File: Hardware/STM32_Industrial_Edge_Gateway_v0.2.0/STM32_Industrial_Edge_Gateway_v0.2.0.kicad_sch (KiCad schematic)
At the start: 75 parts, among them J1 DC Barrel Jack (5.5 × 2.1mm), J2 Conn_01x05, J3 Conn_01x02, J4 RJ45_Hanrun_HR911105A_Horizon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, J5 Screw_Terminal_01x02, J6 DM3AT-SF-PEJM5, Q1 AO3407A, SW1 SW_Push, U1 MP2338GTL, U2 TLV76733DRVR, U3 STM32F407VGTx, U4 SMD3225, U5 LAN8742A, U6 MAX3485ESA_T, Y1 ABM8G-25.000MHZ-B4Y-T3

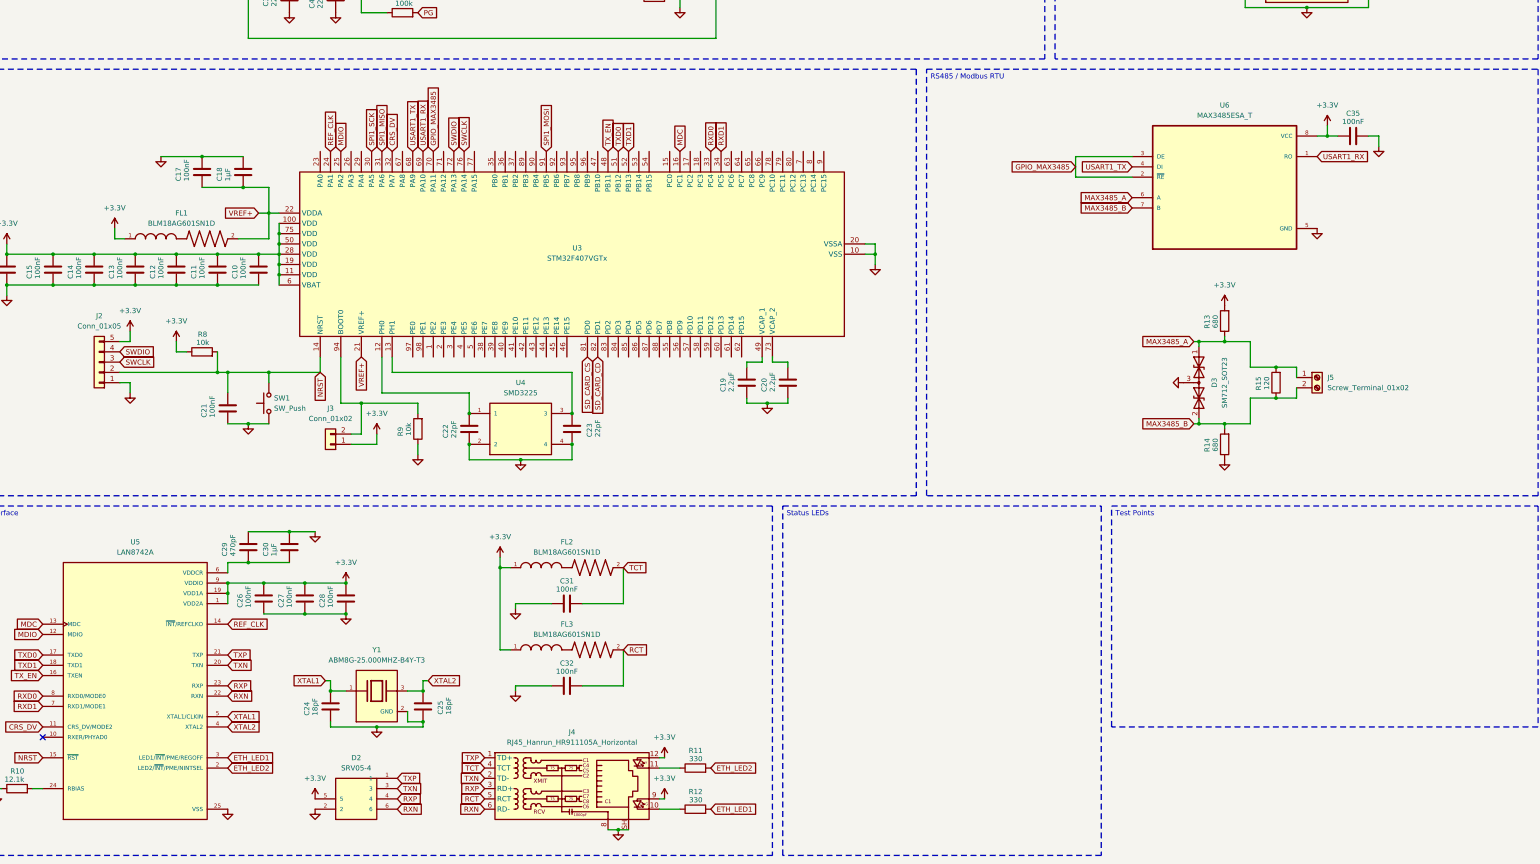
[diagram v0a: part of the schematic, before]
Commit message: Complete Testing Points and Status LEDs schematics
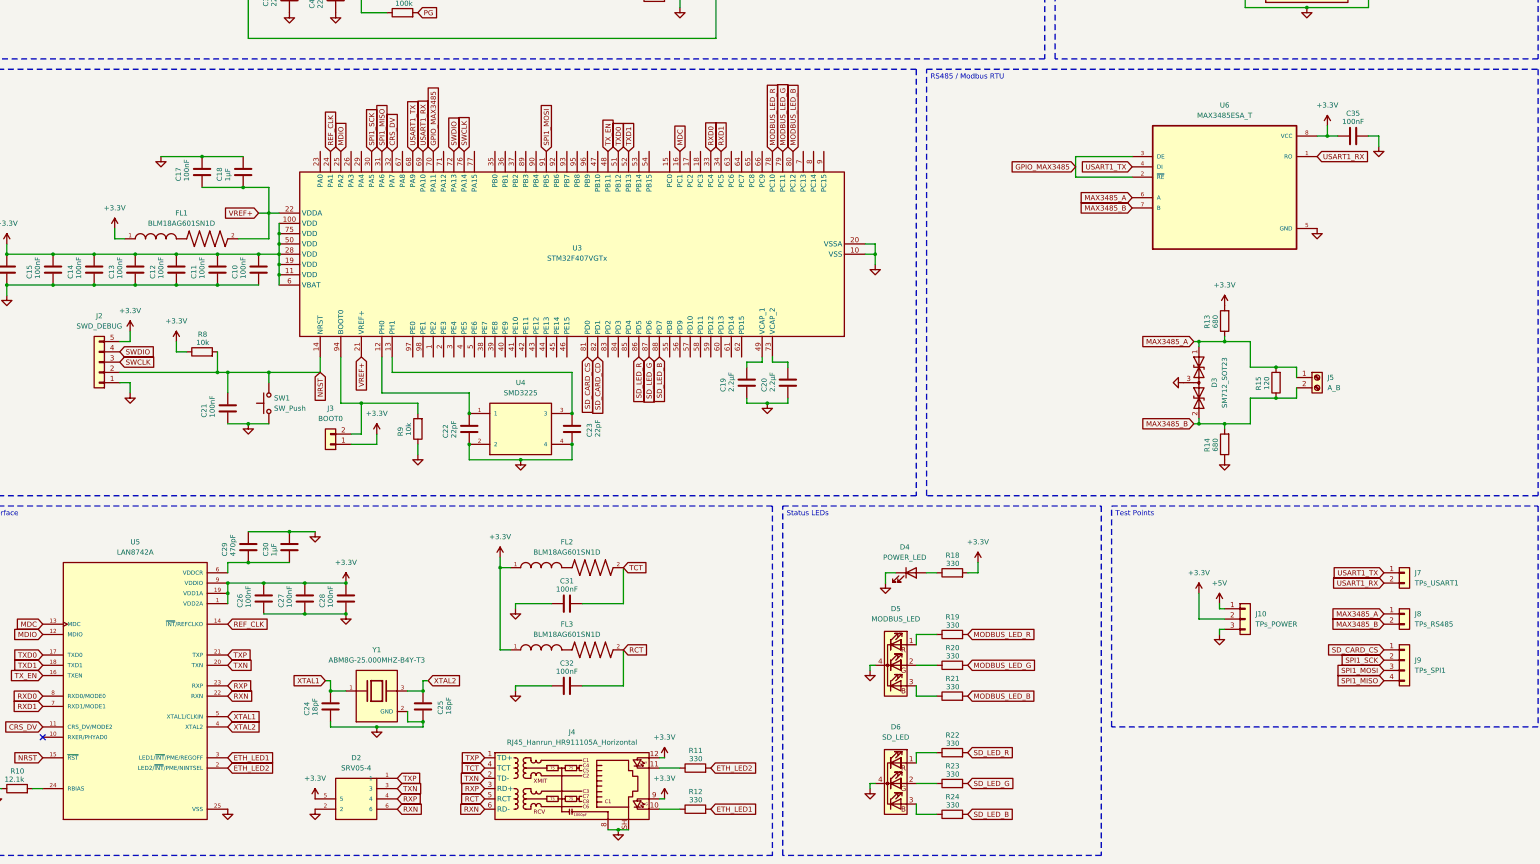
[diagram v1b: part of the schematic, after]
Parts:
- added D4: POWER_LED, symbol Device:LED
- added D5: MODBUS_LED, symbol Device:LED_RGBK
- added D6: SD_LED, symbol Device:LED_RGBK
- added J10: TPs_POWER, symbol Connector_Generic:Conn_01x03
- added J7: TPs_USART1, symbol Connector_Generic:Conn_01x02
- added J8: TPs_RS485, symbol Connector_Generic:Conn_01x02
- added J9: TPs_SPI1, symbol Connector_Generic:Conn_01x04
- added R18, R19, R20, R21, R22, R23, R24: 330, Resistor_SMD:R_0603_1608Metric, symbol Device:R
- J2: value Conn_01x05 -> SWD_DEBUG
- J3: value Conn_01x02 -> BOOT0
- J5: value Screw_Terminal_01x02 -> A_B
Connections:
- net +3.3V: now also J10.2 (Pin_2), R18.2
- net +5V: now also J10.1 (Pin_1)
- net GND: now also D4.1 (K), D5.4 (K), D6.4 (K), J10.3 (Pin_3)
- net MAX3485_A: now also J8.1 (Pin_1)
- net MAX3485_B: now also J8.2 (Pin_2)
- net SD_CARD_CS: now also J9.1 (Pin_1)
- net SPI1_MISO: now also J9.4 (Pin_4)
- net SPI1_MOSI: now also J9.3 (Pin_3)
- net SPI1_SCK: now also J9.2 (Pin_2)
- net USART1_RX: now also J7.2 (Pin_2)
- net USART1_TX: now also J7.1 (Pin_1)
- net MODBUS_LED_R: now reaches U3.78 (PC10)
- net MODBUS_LED_R: now also R19.2
- net MODBUS_LED_G: now reaches U3.79 (PC11)
- net MODBUS_LED_G: now also R20.2
- net MODBUS_LED_B: now reaches U3.80 (PC12)
- net MODBUS_LED_B: now also R21.2
- net SD_LED_R: now reaches U3.86 (PD5)
- net SD_LED_R: now also R22.2
- net SD_LED_G: now reaches U3.87 (PD6)
- net SD_LED_G: now also R23.2
- net SD_LED_B: now reaches U3.88 (PD7)
- net SD_LED_B: now also R24.2
- new net: D5.2 (GA), R20.1
- new net: D6.3 (BA), R24.1
- new net: D5.3 (BA), R21.1
- new net: D6.1 (RA), R22.1
- new net: D5.1 (RA), R19.1
- new net: D6.2 (GA), R23.1
- new net: D4.2 (A), R18.1

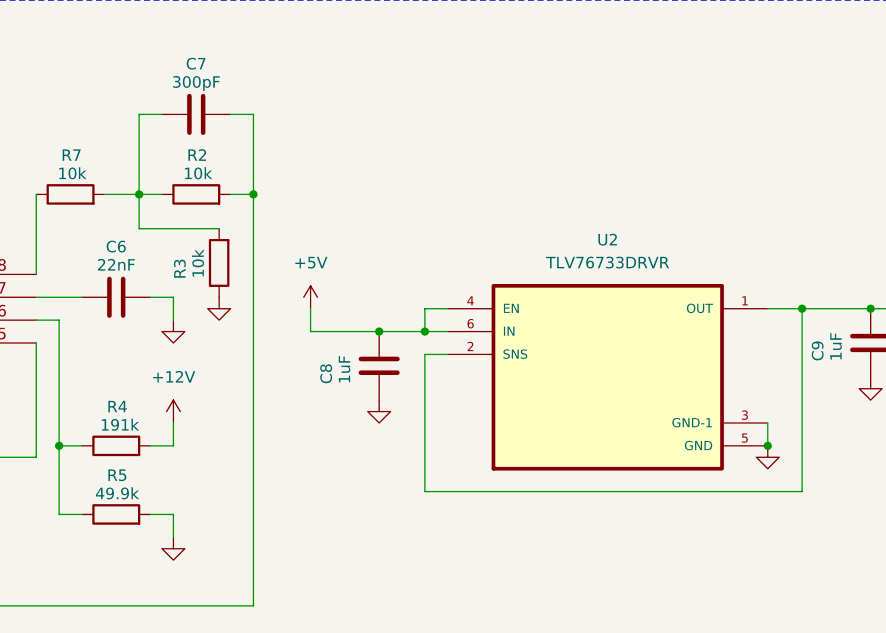
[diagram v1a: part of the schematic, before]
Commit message: Fix and update schematic
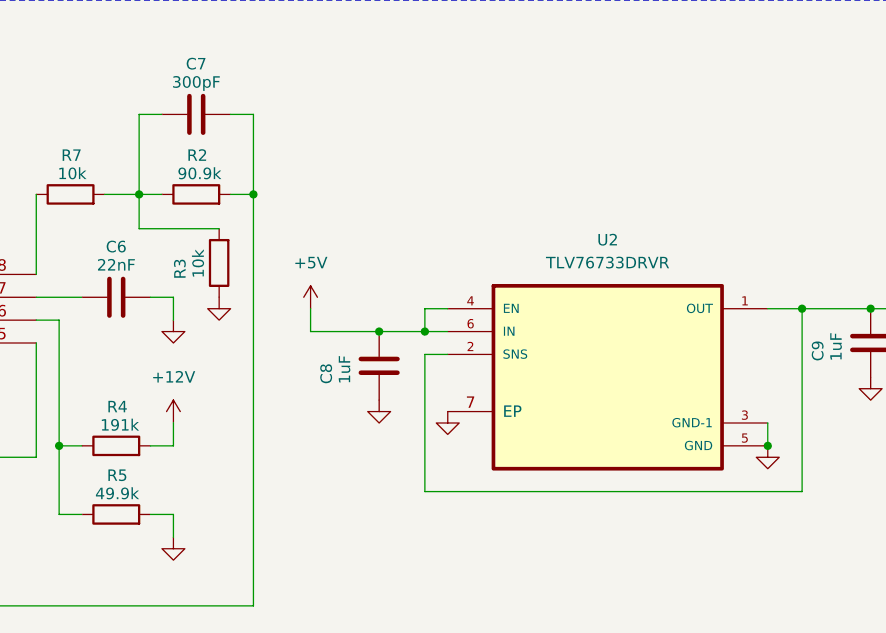
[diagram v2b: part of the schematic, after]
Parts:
- C1, C10, C11, C12, C13, C14, C15, C16, C17, C18, C19, C2, C20, C21, C22, C23, C24, C25, C26, C27, C28, C29, C3, C30, C33, C34, C4, C8, C9: footprint (none) -> Capacitor_SMD:C_0603_1608Metric
- D4: footprint (none) -> LED_SMD:LED_0603_1608Metric
- D5, D6: footprint (none) -> LED_SMD:LED_RGB_1210
- J1: footprint EJ503A:MPD_EJ503A -> DC Barrel Jack (5.5 × 2.1mm):EJ503A
- J10: footprint (none) -> Connector_PinHeader_2.54mm:PinHeader_1x03_P2.54mm_Vertical
- J2: footprint (none) -> Connector_PinHeader_2.54mm:PinHeader_1x05_P2.54mm_Vertical
- J3, J7, J8: footprint (none) -> Connector_PinHeader_2.54mm:PinHeader_1x02_P2.54mm_Vertical
- J5: footprint (none) -> TerminalBlock_Phoenix:TerminalBlock_Phoenix_MKDS-1,5-2-5.08_1x02_P5.08mm_Horizontal
- J9: footprint (none) -> Connector_PinHeader_2.54mm:PinHeader_1x04_P2.54mm_Vertical
- Q1: footprint AO3407A:SOT95P280X125-3N -> AO3407A:AO3407A
- R2: value 10k -> 90.9k
- SW1: footprint (none) -> Button_Switch_SMD:SW_SPST_TL3342
- U1: footprint SOT583_MP2338_MNP -> MP2338GTL:MP2338GTL
- U5: footprint LAN8742A-CZ-TR:QFN50P400X400X100-25N -> LAN8742A:LAN8742A-CZ-TR
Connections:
- net GND: now also U2.7 (EP)
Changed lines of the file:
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@@
 			)
 		)
-		(property "Footprint" ""
+		(property "Footprint" "Capacitor_SMD:C_0603_1608Metric"
 			(at 77.1652 118.11 0)
 			(hide yes)
@@
 			)
 		)
-		(property "Footprint" ""
+		(property "Footprint" "Capacitor_SMD:C_0603_1608Metric"
 			(at 218.1352 58.42 0)
 			(hide yes)
@@
 			)
 		)
-		(property "Footprint" ""
+		(property "Footprint" "Capacitor_SMD:C_0603_1608Metric"
 			(at 129.8448 242.57 0)
 			(hide yes)
@@
 			)
 		)
-		(property "Footprint" ""
+		(property "Footprint" "Connector_PinHeader_2.54mm:PinHeader_1x03_P2.54mm_Vertical"
 			(at 334.01 224.79 0)
 			(hide yes)
@@
 			)
 		)
-		(property "Footprint" "SOT583_MP2338_MNP"
+		(property "Footprint" "MP2338GTL:MP2338GTL"
 			(at 138.43 44.45 0)
 			(hide yes)
@@
 			)
 		)
-		(property "Footprint" ""
+		(property "Footprint" "Capacitor_SMD:C_0603_1608Metric"
 			(at 378.1552 41.91 0)
 			(hide yes)
@@
 			)
 		)
-		(property "Footprint" ""
+		(property "Footprint" "Button_Switch_SMD:SW_SPST_TL3342"
 			(at 87.63 171.45 0)
 			(hide yes)
@@
 			)
 		)
-		(property "Footprint" ""
+		(property "Footprint" "Capacitor_SMD:C_0603_1608Metric"
 			(at 98.7552 210.82 0)
 			(hide yes)
@@
 			)
 		)
-		(property "Footprint" ""
+		(property "Footprint" "TerminalBlock_Phoenix:TerminalBlock_Phoenix_MKDS-1,5-2-5.08_1x02_P5.08mm_Horizontal"
 			(at 351.79 165.1 0)
 			(hide yes)
@@
 			)
 		)
-		(property "Value" "10k"
-			(at 198.628 33.274 90)
+		(property "Value" "90.9k"
+			(at 199.644 33.274 90)
 			(show_name no)
 			(do_not_autoplace no)
@@
 			)
 		)
-		(property "Footprint" ""
+		(property "Footprint" "Capacitor_SMD:C_0603_1608Metric"
 			(at 108.9152 250.19 0)
 			(hide yes)
@@
 			)
 		)
-		(property "Footprint" ""
+		(property "Footprint" "Capacitor_SMD:C_0603_1608Metric"
 			(at 116.5352 54.61 0)
 			(hide yes)
@@
 			)
 		)
-		(property "Footprint" ""
+		(property "Footprint" "Capacitor_SMD:C_0603_1608Metric"
 			(at 367.9952 41.91 0)
 			(hide yes)
@@
 		(pin "1"
 		)
+		(pin "7"
+		)
 		(instances
 			(project "STM32_Industrial_Edge_Gateway_v0.2.0"
@@
 	(symbol
 		(lib_id "power:GND")
+		(at 224.79 59.69 0)
+		(unit 1)
+		(body_style 1)
+		(exclude_from_sim no)
+		(in_bom yes)
+		(on_board yes)
+		(in_pos_files yes)
+		(dnp no)
+		(fields_autoplaced yes)
+		(property "Reference" "#PWR082"
+			(at 224.79 66.04 0)
+			(hide yes)
+			(show_name no)
+			(do_not_autoplace no)
+			(effects
+				(font
+					(size 1.27 1.27)
+				)
+			)
+		)
+		(property "Value" "GND"
+			(at 224.79 64.77 0)
+			(hide yes)
+			(show_name no)
+			(do_not_autoplace no)
+			(effects
+				(font
+					(size 1.27 1.27)
+				)
+			)
+		)
+		(property "Footprint" ""
+			(at 224.79 59.69 0)
+			(hide yes)
+			(show_name no)
+			(do_not_autoplace no)
+			(effects
+				(font
+					(size 1.27 1.27)
+				)
+			)
+		)
+		(property "Datasheet" ""
+			(at 224.79 59.69 0)
+			(hide yes)
+			(show_name no)
+			(do_not_autoplace no)
+			(effects
+				(font
+					(size 1.27 1.27)
+				)
+			)
+		)
+		(property "Description" "Power symbol creates a global label with name \"GND\" , ground"
+			(at 224.79 59.69 0)
+			(hide yes)
+			(show_name no)
+			(do_not_autoplace no)
+			(effects
+				(font
+					(size 1.27 1.27)
+				)
+			)
+		)
+		(pin "1"
+		)
+		(instances
+			(project "STM32_Industrial_Edge_Gateway_v0.2.0"
+				(path "/abc15c43-296c-4c96-9fe3-be02bbc91336"
+					(reference "#PWR082")
+					(unit 1)
+				)
+			)
+		)
+	)
+	(symbol
+		(lib_id "power:GND")
 		(at 153.67 242.57 0)
 		(unit 1)
@@
 			)
 		)
-		(property "Footprint" "AO3407A:SOT95P280X125-3N"
+		(property "Footprint" "AO3407A:AO3407A"
 			(at 90.17 45.72 0)
 			(hide yes)
@@
 			)
 		)
-		(property "Footprint" ""
+		(property "Footprint" "Connector_PinHeader_2.54mm:PinHeader_1x04_P2.54mm_Vertical"
 			(at 373.38 234.95 0)
 			(hide yes)
@@
 			)
 		)
-		(property "Footprint" ""
+		(property "Footprint" "Capacitor_SMD:C_0603_1608Metric"
 			(at 166.6748 173.99 0)
 			(hide yes)
@@
 			)
 		)
-		(property "Footprint" ""
+		(property "Footprint" "Capacitor_SMD:C_0603_1608Metric"
 			(at 110.1852 74.93 0)
 			(hide yes)
@@
 			)
 		)
-		(property "Footprint" ""
+		(property "Footprint" "Connector_PinHeader_2.54mm:PinHeader_1x02_P2.54mm_Vertical"
 			(at 373.38 223.52 0)
 			(hide yes)
@@
 			)
 		)
-		(property "Footprint" ""
+		(property "Footprint" "Capacitor_SMD:C_0603_1608Metric"
 			(at 28.9052 142.24 0)
 			(hide yes)
@@
 			)
 		)
-		(property "Footprint" ""
+		(property "Footprint" "Connector_PinHeader_2.54mm:PinHeader_1x05_P2.54mm_Vertical"
 			(at 50.8 161.29 0)
 			(hide yes)
@@
 			)
 		)
-		(property "Footprint" ""
+		(property "Footprint" "Capacitor_SMD:C_0603_1608Metric"
 			(at 221.9452 170.18 0)
 			(hide yes)
@@
 			)
 		)
-		(property "Footprint" ""
+		(property "Footprint" "Capacitor_SMD:C_0603_1608Metric"
 			(at 40.3352 142.24 0)
 			(hide yes)
@@
 			)
 		)
-		(property "Footprint" ""
+		(property "Footprint" "Capacitor_SMD:C_0603_1608Metric"
 			(at 60.6552 142.24 0)
 			(hide yes)
@@
 			)
 		)
-		(property "Footprint" ""
+		(property "Footprint" "Capacitor_SMD:C_0603_1608Metric"
 			(at 127.9652 54.61 0)
 			(hide yes)
@@
 			)
 		)
-		(property "Footprint" ""
+		(property "Footprint" "Capacitor_SMD:C_0603_1608Metric"
 			(at 91.1352 142.24 0)
 			(hide yes)
@@
 			)
 		)
-		(property "Footprint" ""
+		(property "Footprint" "Capacitor_SMD:C_0603_1608Metric"
 			(at 88.5952 210.82 0)
 			(hide yes)
@@
 			)
 		)
-		(property "Footprint" ""
+		(property "Footprint" "Capacitor_SMD:C_0603_1608Metric"
 			(at 102.5652 223.52 0)
 			(hide yes)
@@
 			)
 		)
-		(property "Footprint" ""
+		(property "Footprint" "Capacitor_SMD:C_0603_1608Metric"
 			(at 87.3252 118.11 0)
 			(hide yes)
@@
 			)
 		)
-		(property "Footprint" ""
+		(property "Footprint" "Capacitor_SMD:C_0603_1608Metric"
 			(at 211.7852 170.18 0)
 			(hide yes)
@@
 			)
 		)
-		(property "Footprint" ""
+		(property "Footprint" "Capacitor_SMD:C_0603_1608Metric"
 			(at 143.2052 181.61 0)
 			(hide yes)
@@
 			)
 		)
-		(property "Footprint" ""
+		(property "Footprint" "Capacitor_SMD:C_0603_1608Metric"
 			(at 98.7552 74.93 0)
 			(hide yes)
@@
 			)
 		)
-		(property "Footprint" ""
+		(property "Footprint" "LED_SMD:LED_RGB_1210"
 			(at 247.65 237.49 0)
 			(hide yes)
@@
 			)
 		)
-		(property "Footprint" "LAN8742A-CZ-TR:QFN50P400X400X100-25N"
+		(property "Footprint" "LAN8742A:LAN8742A-CZ-TR"
 			(at 59.69 243.84 0)
 			(hide yes)
@@
 			)
 		)
-		(property "Footprint" ""
+		(property "Footprint" "Capacitor_SMD:C_0603_1608Metric"
 			(at 272.7452 55.88 0)
 			(hide yes)
@@
 			)
 		)
-		(property "Footprint" ""
+		(property "Footprint" "Capacitor_SMD:C_0603_1608Metric"
 			(at 83.5152 176.53 0)
 			(hide yes)
@@
 			)
 		)
-		(property "Footprint" "EJ503A:MPD_EJ503A"
+		(property "Footprint" "DC Barrel Jack (5.5 × 2.1mm):EJ503A"
 			(at 36.83 45.72 0)
 			(hide yes)
@@
 			)
 		)
-		(property "Footprint" ""
+		(property "Footprint" "Capacitor_SMD:C_0603_1608Metric"
 			(at 70.8152 142.24 0)
 			(hide yes)
@@
 			)
 		)
-		(property "Footprint" ""
+		(property "Footprint" "Connector_PinHeader_2.54mm:PinHeader_1x02_P2.54mm_Vertical"
 			(at 373.38 213.36 0)
 			(hide yes)
@@
 			)
 		)
-		(property "Footprint" ""
+		(property "Footprint" "Capacitor_SMD:C_0603_1608Metric"
 			(at 112.7252 223.52 0)
 			(hide yes)
@@
 			)
 		)
-		(property "Footprint" ""
+		(property "Footprint" "Capacitor_SMD:C_0603_1608Metric"
 			(at 80.9752 142.24 0)
 			(hide yes)
@@
 			)
 		)
-		(property "Footprint" ""
+		(property "Footprint" "Connector_PinHeader_2.54mm:PinHeader_1x02_P2.54mm_Vertical"
 			(at 107.95 181.61 0)
 			(hide yes)
@@
 			)
 		)
-		(property "Footprint" ""
+		(property "Footprint" "LED_SMD:LED_0603_1608Metric"
 			(at 251.46 213.36 0)
 			(hide yes)
@@
 			)
 		)
-		(property "Footprint" ""
+		(property "Footprint" "Capacitor_SMD:C_0603_1608Metric"
 			(at 50.4952 142.24 0)
 			(hide yes)
@@
 			)
 		)
-		(property "Footprint" ""
+		(property "Footprint" "LED_SMD:LED_RGB_1210"
 			(at 247.65 266.7 0)
 			(hide yes)
@@
 			)
 		)
-		(property "Footprint" ""
+		(property "Footprint" "Capacitor_SMD:C_0603_1608Metric"
 			(at 92.4052 223.52 0)
 			(hide yes)
